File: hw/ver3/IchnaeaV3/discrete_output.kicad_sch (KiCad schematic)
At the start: 2 parts, among them U11 74HC595, U17 74HC595

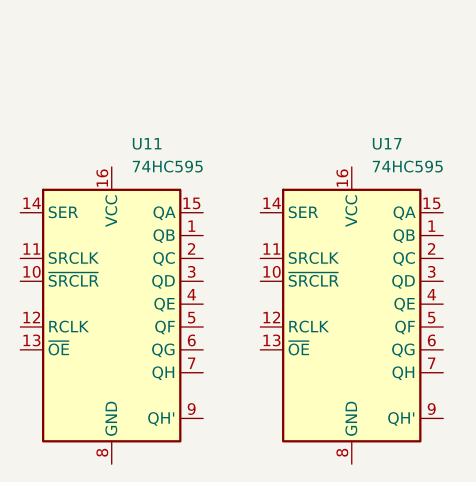
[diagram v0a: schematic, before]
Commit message: Experiment with a new power stage layout
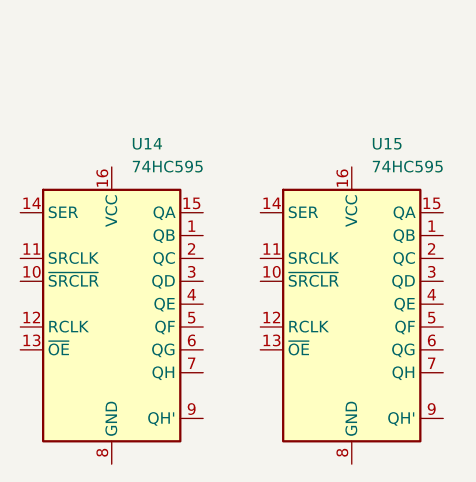
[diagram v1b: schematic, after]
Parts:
- renumbered U11 to U14, U17 to U15
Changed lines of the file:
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@@
 		(dnp no)
 		(fields_autoplaced yes)
-		(property "Reference" "U11"
+		(property "Reference" "U14"
 			(at 135.5441 69.85 0)
 			(effects
@@
 			(project "IchnaeaV3"
 				(path "/93408532-1ffa-463d-873c-16289d2b7987/f8cdf9d7-add1-4ff8-8430-918a71e3d1f9/fdf9ed79-d6dc-4b90-81da-ef64aa580205"
-					(reference "U11")
+					(reference "U14")
 					(unit 1)
 				)
@@
 		(dnp no)
 		(fields_autoplaced yes)
-		(property "Reference" "U17"
+		(property "Reference" "U15"
 			(at 162.2141 69.85 0)
 			(effects
@@
 			(project "IchnaeaV3"
 				(path "/93408532-1ffa-463d-873c-16289d2b7987/f8cdf9d7-add1-4ff8-8430-918a71e3d1f9/fdf9ed79-d6dc-4b90-81da-ef64aa580205"
-					(reference "U17")
+					(reference "U15")
 					(unit 1)
 				)

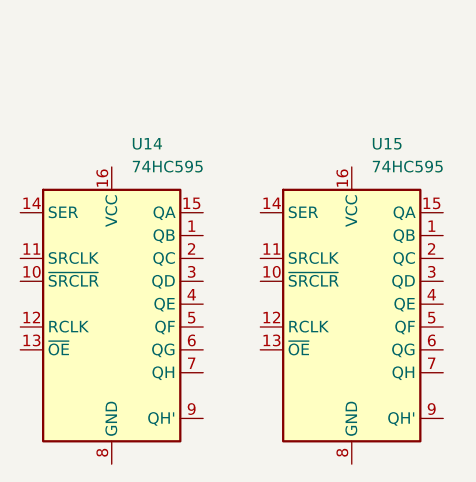
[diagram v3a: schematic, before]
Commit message: Improve more of the power stage layout
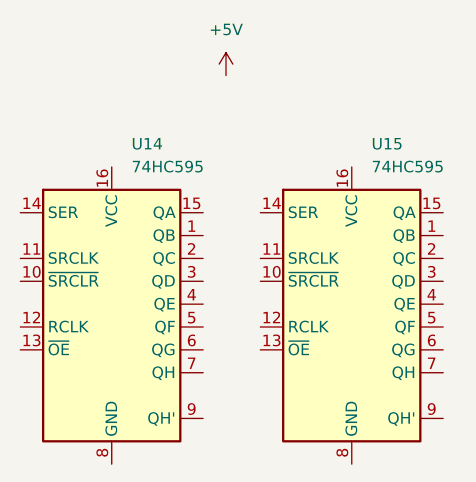
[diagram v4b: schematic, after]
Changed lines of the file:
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@@
+			)
+		)
+		(property "DigiKey" ""
+			(at 133.35 87.63 0)
+			(effects
+				(font
+					(size 1.27 1.27)
+				)
+				(hide yes)
 			)
 		)
@@
 			)
 		)
+		(property "DigiKey" ""
+			(at 160.02 87.63 0)
+			(effects
+				(font
+					(size 1.27 1.27)
+				)
+				(hide yes)
+			)
+		)
 		(pin "7"
 		)
@@
 					(unit 1)
 				)
+			)
+		)
+	)
+	(symbol
+		(lib_id "power:+5V")
+		(at 146.05 62.23 0)
+		(unit 1)
+		(exclude_from_sim no)
+		(in_bom yes)
+		(on_board yes)
+		(dnp no)
+		(fields_autoplaced yes)
+		(property "Reference" "#PWR083"
+			(at 146.05 66.04 0)
+			(effects
+				(font
+					(size 1.27 1.27)
+				)
+				(hide yes)
+			)
+		)
+		(property "Value" "+5V"
+			(at 146.05 57.15 0)
+			(effects
+				(font
+					(size 1.27 1.27)
+				)
+			)
+		)
+		(property "Footprint" ""
+			(at 146.05 62.23 0)
+			(effects
+				(font
+					(size 1.27 1.27)
+				)
+				(hide yes)
+			)
+		)
+		(property "Datasheet" ""
+			(at 146.05 62.23 0)
+			(effects
+				(font
+					(size 1.27 1.27)
+				)
+				(hide yes)
+			)
+		)
+		(property "Description" "Power symbol creates a global label with name \"+5V\""
+			(at 146.05 62.23 0)
+			(effects
+				(font
+					(size 1.27 1.27)
+				)
+				(hide yes)
+			)
+		)
+		(pin "1"
+		)
+		(instances
+			(project "IchnaeaV3"
+				(path "/93408532-1ffa-463d-873c-16289d2b7987/f8cdf9d7-add1-4ff8-8430-918a71e3d1f9/fdf9ed79-d6dc-4b90-81da-ef64aa580205"
+					(reference "#PWR083")
+					(unit 1)
+				)
